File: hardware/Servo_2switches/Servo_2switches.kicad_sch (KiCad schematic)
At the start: 12 parts, among them M1 Motor_Servo, SW1 SW_Push, U1 ESP32, U2 ACS712, U3 5V-PS

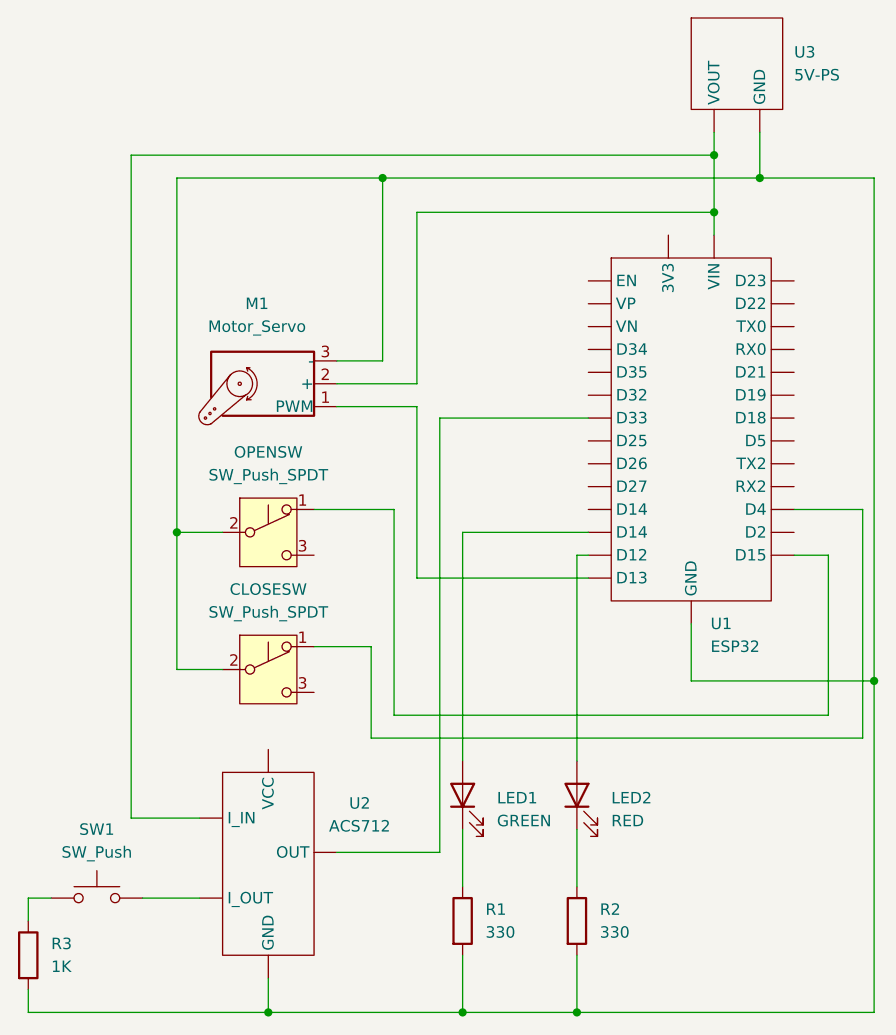
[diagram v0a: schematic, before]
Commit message: Corrected schematic
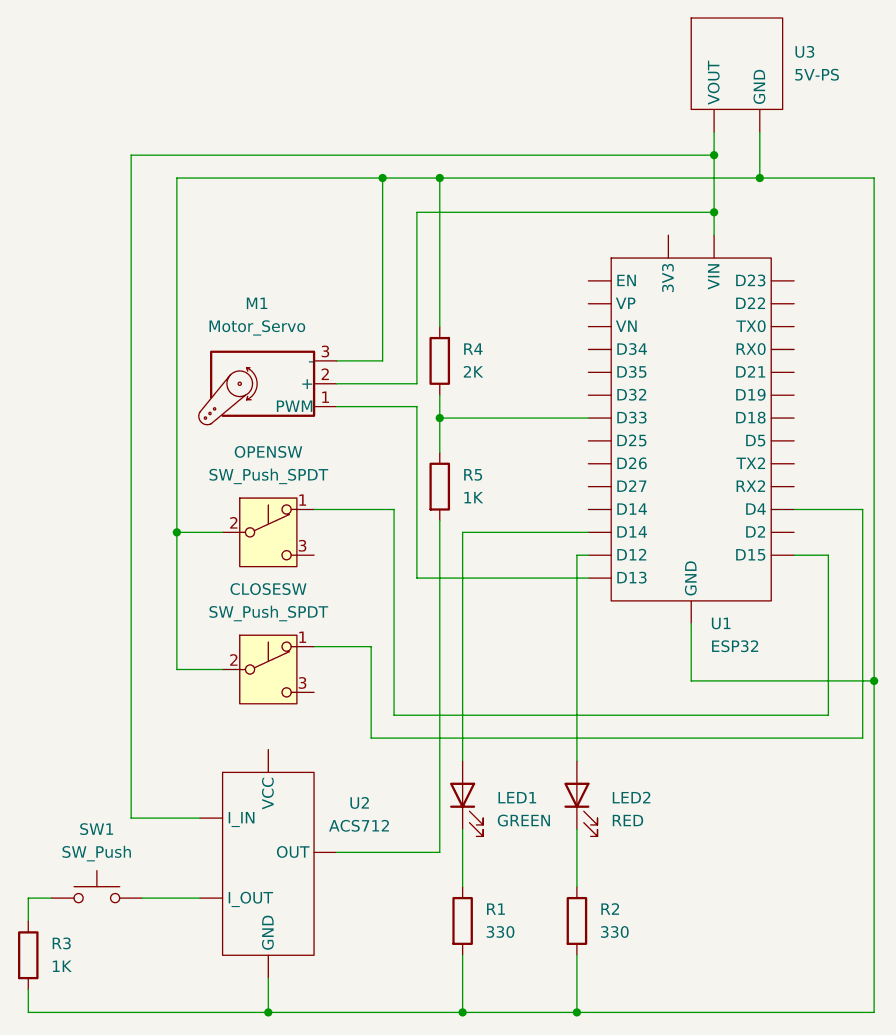
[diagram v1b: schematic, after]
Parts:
- added R4: 2K, symbol Device:R
- added R5: 1K, symbol Device:R
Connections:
- net at CLOSESW.2 (B), M1.3 (-), OPENSW.2 (B)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: now also R4.2
- net at U1. (D15): now also M1.1 (PWM); no longer U2. (OUT)
- new net: R4.1, R5.1, U1. (D15)
- new net: R5.2, U2. (OUT)
